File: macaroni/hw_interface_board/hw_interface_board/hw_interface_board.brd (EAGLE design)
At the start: 64.8 x 40.3 mm, 19 parts, among them M1 455-1750-1-ND, M2 455-1750-1-ND, M3 455-1750-1-ND

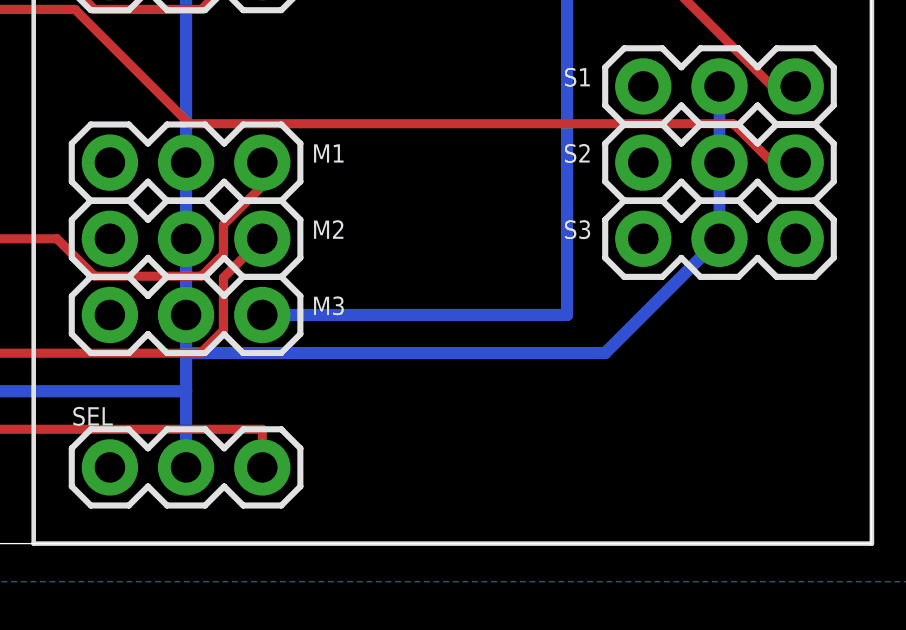
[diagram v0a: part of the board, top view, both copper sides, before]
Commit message: Fixes clearance issues based on Seeed Studios DRU
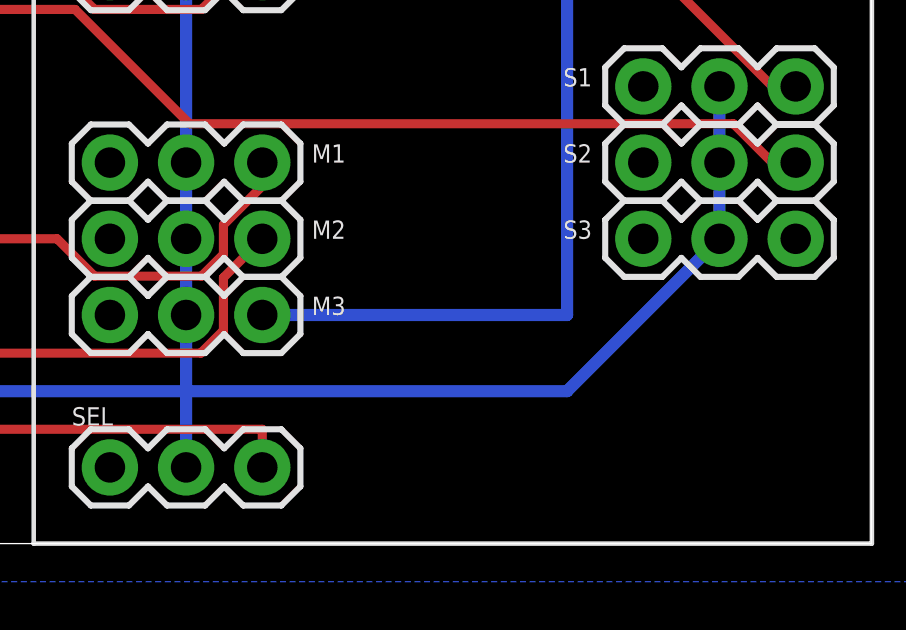
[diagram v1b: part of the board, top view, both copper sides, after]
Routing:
- net VCC: track 88.3 -> 88.9 mm
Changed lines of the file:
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@@
 </class>
 </classes>
-<designrules name="default">
+<designrules name="SeeedStudio_2layer_DRU_no_angle_20140221">
 <description language="de">&lt;b&gt;EAGLE Design Rules&lt;/b&gt;
 &lt;p&gt;
@@
 necessary adjustments and save your customized
 design rules under a new name.</description>
+<description language="zh">&lt;b&gt;Seeed Studio EAGLE Design Rules&lt;/b&gt;
+</description>
 <param name="layerSetup" value="(1*16)"/>
-<param name="mtCopper" value="0.035mm 0.035mm 0.035mm 0.035mm 0.035mm 0.035mm 0.035mm 0.035mm 0.035mm 0.035mm 0.035mm 0.035mm 0.035mm 0.035mm 0.035mm 0.035mm"/>
-<param name="mtIsolate" value="1.5mm 0.15mm 0.2mm 0.15mm 0.2mm 0.15mm 0.2mm 0.15mm 0.2mm 0.15mm 0.2mm 0.15mm 0.2mm 0.15mm 0.2mm"/>
+<param name="mtCopper" value="0.035mm 0.0175mm 0.035mm 0.035mm 0.035mm 0.035mm 0.035mm 0.035mm 0.035mm 0.035mm 0.035mm 0.035mm 0.035mm 0.035mm 0.0175mm 0.035mm"/>
+<param name="mtIsolate" value="1.5mm 1.1mm 0.2mm 0.15mm 0.2mm 0.15mm 0.2mm 0.15mm 0.2mm 0.15mm 0.2mm 0.15mm 0.2mm 0.15mm 0.2mm"/>
 <param name="mdWireWire" value="6mil"/>
 <param name="mdWirePad" value="6mil"/>
@@
 <param name="mdPadVia" value="6mil"/>
 <param name="mdViaVia" value="6mil"/>
-<param name="mdSmdPad" value="6mil"/>
-<param name="mdSmdVia" value="6mil"/>
-<param name="mdSmdSmd" value="6mil"/>
-<param name="mdViaViaSameLayer" value="6mil"/>
+<param name="mdSmdPad" value="0mil"/>
+<param name="mdSmdVia" value="0mil"/>
+<param name="mdSmdSmd" value="0mil"/>
+<param name="mdViaViaSameLayer" value="8mil"/>
 <param name="mnLayersViaInSmd" value="2"/>
-<param name="mdCopperDimension" value="40mil"/>
-<param name="mdDrill" value="6mil"/>
+<param name="mdCopperDimension" value="10mil"/>
+<param name="mdDrill" value="10mil"/>
 <param name="mdSmdStop" value="0mil"/>
 <param name="msWidth" value="6mil"/>
-<param name="msDrill" value="0.35mm"/>
-<param name="msMicroVia" value="9.99mm"/>
+<param name="msDrill" value="12mil"/>
+<param name="msMicroVia" value="12mil"/>
 <param name="msBlindViaRatio" value="0.5"/>
 <param name="rvPadTop" value="0.25"/>
@@
 <param name="rlMinPadBottom" value="10mil"/>
 <param name="rlMaxPadBottom" value="20mil"/>
-<param name="rlMinViaOuter" value="8mil"/>
+<param name="rlMinViaOuter" value="6mil"/>
 <param name="rlMaxViaOuter" value="20mil"/>
-<param name="rlMinViaInner" value="8mil"/>
+<param name="rlMinViaInner" value="6mil"/>
 <param name="rlMaxViaInner" value="20mil"/>
 <param name="rlMinMicroViaOuter" value="4mil"/>
@@
 <param name="psTop" value="-1"/>
 <param name="psBottom" value="-1"/>
-<param name="psFirst" value="-1"/>
+<param name="psFirst" value="0"/>
 <param name="psElongationLong" value="100"/>
 <param name="psElongationOffset" value="100"/>
 <param name="mvStopFrame" value="1"/>
 <param name="mvCreamFrame" value="0"/>
-<param name="mlMinStopFrame" value="4mil"/>
-<param name="mlMaxStopFrame" value="4mil"/>
+<param name="mlMinStopFrame" value="2mil"/>
+<param name="mlMaxStopFrame" value="2mil"/>
 <param name="mlMinCreamFrame" value="0mil"/>
 <param name="mlMaxCreamFrame" value="0mil"/>
-<param name="mlViaStopLimit" value="0mil"/>
+<param name="mlViaStopLimit" value="100mil"/>
 <param name="srRoundness" value="0"/>
 <param name="srMinRoundness" value="0mil"/>
@@
 <param name="checkAngle" value="0"/>
 <param name="checkFont" value="1"/>
-<param name="checkRestrict" value="1"/>
+<param name="checkRestrict" value="0"/>
 <param name="checkStop" value="0"/>
 <param name="checkValues" value="0"/>
@@
 <contactref element="S3" pad="2"/>
 <wire x1="41.91" y1="2.54" x2="41.91" y2="5.08" width="0.4064" layer="16"/>
-<wire x1="41.91" y1="5.08" x2="41.91" y2="6.35" width="0.4064" layer="16"/>
-<wire x1="41.91" y1="6.35" x2="41.91" y2="7.62" width="0.4064" layer="16"/>
+<wire x1="41.91" y1="5.08" x2="41.91" y2="7.62" width="0.4064" layer="16"/>
 <wire x1="41.91" y1="7.62" x2="41.91" y2="10.16" width="0.4064" layer="16"/>
 <wire x1="41.91" y1="12.7" x2="41.91" y2="19.05" width="0.4064" layer="16"/>
@@
 <wire x1="59.69" y1="15.24" x2="59.69" y2="12.7" width="0.4064" layer="16"/>
 <wire x1="59.69" y1="12.7" x2="59.69" y2="10.16" width="0.4064" layer="16"/>
-<wire x1="59.69" y1="10.16" x2="55.88" y2="6.35" width="0.4064" layer="16"/>
-<wire x1="55.88" y1="6.35" x2="41.91" y2="6.35" width="0.4064" layer="16"/>
 <wire x1="29.21" y1="2.54" x2="29.21" y2="5.08" width="0.4064" layer="16"/>
 <wire x1="29.21" y1="5.08" x2="29.21" y2="6.35" width="0.4064" layer="16"/>
@@
 <wire x1="31.213425" y1="33.0454" x2="29.21" y2="35.048825" width="0.4064" layer="1"/>
 <wire x1="29.21" y1="35.048825" x2="29.21" y2="36.83" width="0.4064" layer="1"/>
+<wire x1="59.69" y1="10.16" x2="54.61" y2="5.08" width="0.4064" layer="16"/>
+<wire x1="54.61" y1="5.08" x2="41.91" y2="5.08" width="0.4064" layer="16"/>
 </signal>
 <signal name="RC3">
